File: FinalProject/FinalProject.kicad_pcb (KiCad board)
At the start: 4 copper layers, 100 x 100 mm, 143 parts, among them J1 GSB4111312HR, J10 Conn_01x02, J2 GSB4111312HR, J3 GSB4111312HR, J5 ARJM11D7-502-AB-EW2, J6 DCJ200-10-A-XX-K_REVA, J7 Conn_01x02, J9 Conn_01x03, Q1 NTTFS5C673NLTAG, Q2 NTTFS5C673NLTAG, SW2 SW_Push, U1 RTL8153B-VB-CG, U11 RP2040, U12 TUSB8041, U14 NCP1117-3.3_SOT223, U15 VEML6040, U16 MAX98357A, U2 TPS2561DRCR, U3 LM74700, U4 TPS62902RPJR, U5 LM74700, U8 ABM8-272-T3, U9 W25Q128JVS, Y2 ABLS-25.000MHZ-B2F-T, Y3 ABM3C-24.000MHZ-D4Y-T

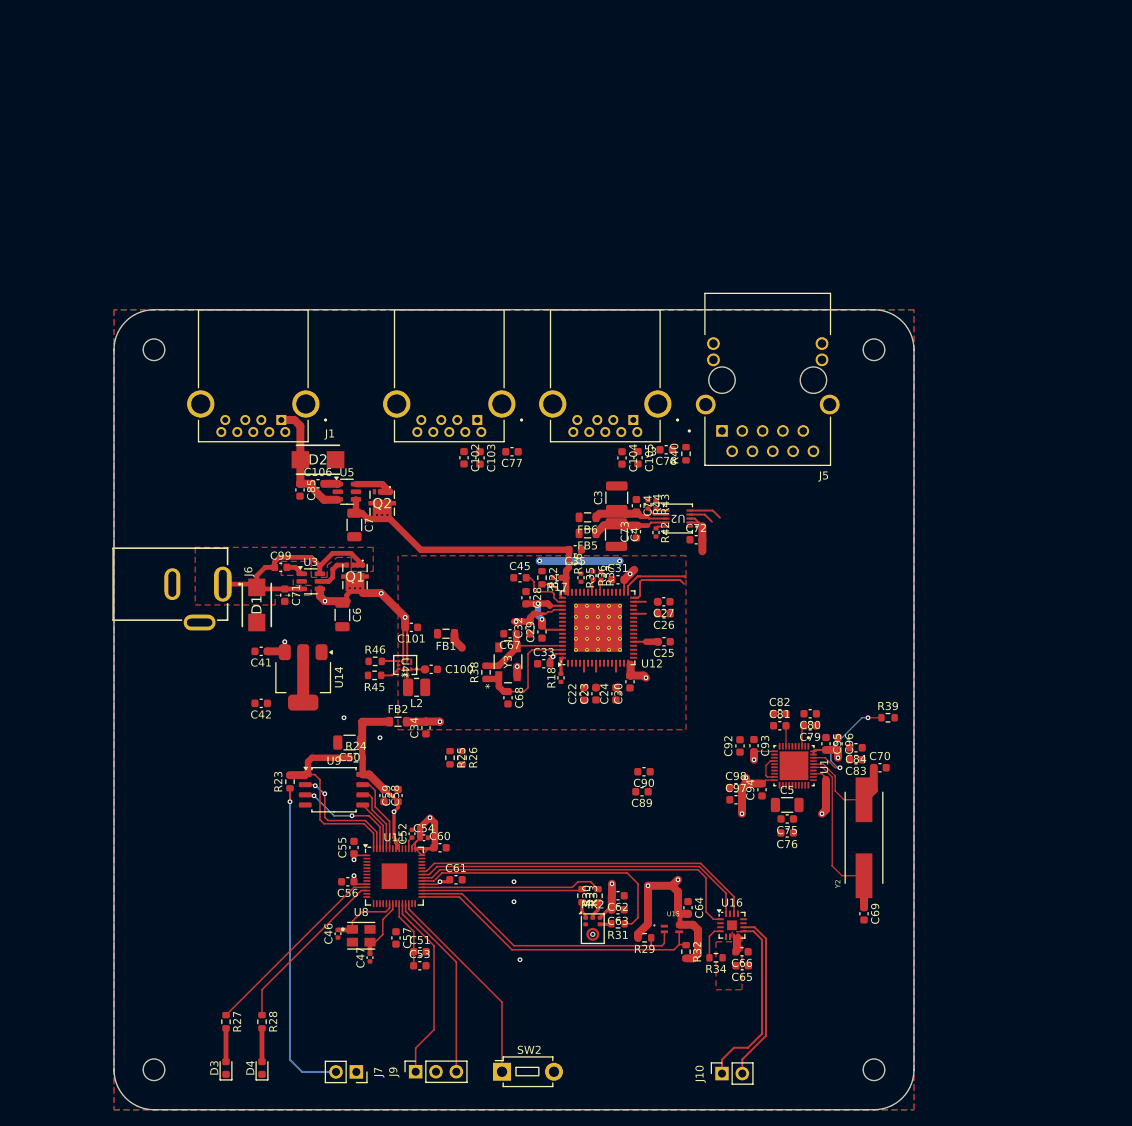
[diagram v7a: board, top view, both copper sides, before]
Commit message: connected all components but having DRC error
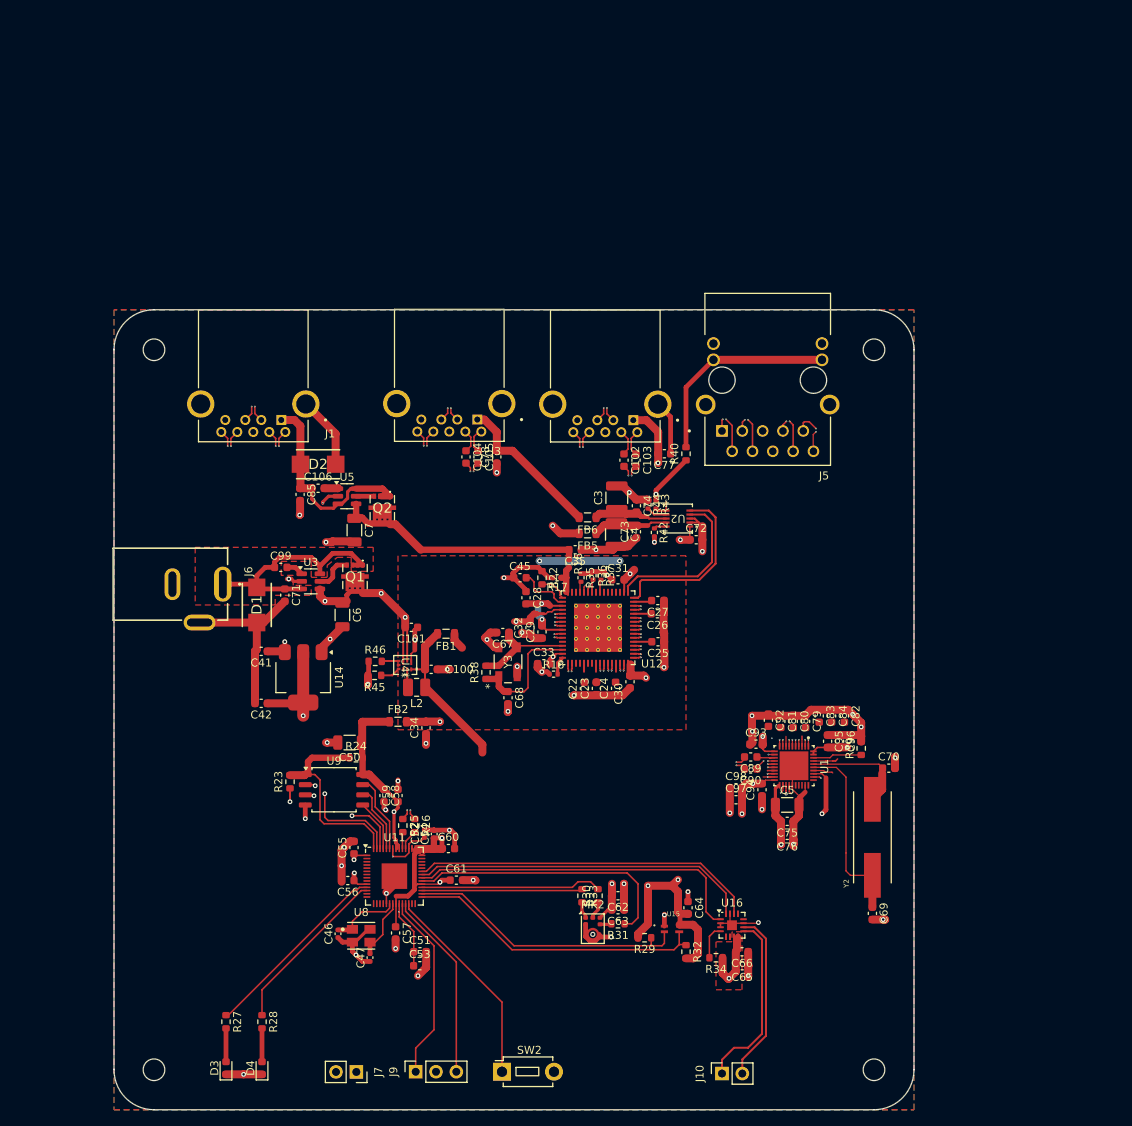
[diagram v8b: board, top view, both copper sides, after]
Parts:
- moved C78 21.2 mm to (72.8, 68.4), turned to 90 degrees
- moved C102 20.0 mm to (88.8, 68.8)
- moved C105 20.0 mm to (70.5, 68.4)
- moved C103 19.5 mm to (90.2, 68.8)
- moved C104 19.5 mm to (69.0, 68.4)
- moved J3 19.5 mm to (66.9, 61.7)
- moved J2 19.5 mm to (86.4, 61.8)
- moved C77 19.1 mm to (93.8, 68.0)
- moved C89 14.3 mm to (104.6, 105.9)
- moved C90 13.3 mm to (104.6, 107.4)
- moved R25 10.3 mm to (61.1, 114.5)
- moved R26 10.3 mm to (62.6, 114.5)
- moved C82 8.08 mm to (116.3, 100.8), turned to -90 degrees
- moved C83 7.15 mm to (113.2, 100.8), turned to -90 degrees
- moved R39 5.08 mm to (118.4, 104.8), turned to 90 degrees
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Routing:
- net GND: track 1.20 -> 228.5 mm, vias 1 -> 50
- net /TD1-: track 0.00 -> 90.1 mm, vias 0 -> 2
- net /TD1+: track 0.00 -> 88.6 mm, vias 0 -> 2
- net /TD2-: track 0.00 -> 82.9 mm, vias 0 -> 2
- net /TD2+: track 0.00 -> 81.5 mm, vias 0 -> 2
- net /ETH_LED0: track 0.00 -> 71.8 mm, vias 0 -> 1
- net /DN2_D+: track 0.00 -> 68.1 mm, vias 0 -> 2
- net /ETH_LED2: track 0.00 -> 67.4 mm, vias 0 -> 1
- net /DN2_D-: track 0.00 -> 65.9 mm, vias 0 -> 2
- net /DN3_D+: track 0.00 -> 65.7 mm, vias 0 -> 2
- net /DN3_D-: track 0.00 -> 63.7 mm, vias 0 -> 2
- net /TD3-: track 0.00 -> 60.3 mm, vias 0 -> 2
- net /TD3+: track 0.00 -> 59.3 mm, vias 0 -> 2
- net /UP_RXN: track 0.00 -> 57.1 mm, vias 0 -> 2
- net /UP_D+: track 0.00 -> 56.5 mm, vias 0 -> 2
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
